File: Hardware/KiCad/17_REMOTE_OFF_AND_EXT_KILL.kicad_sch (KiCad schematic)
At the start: 0 parts

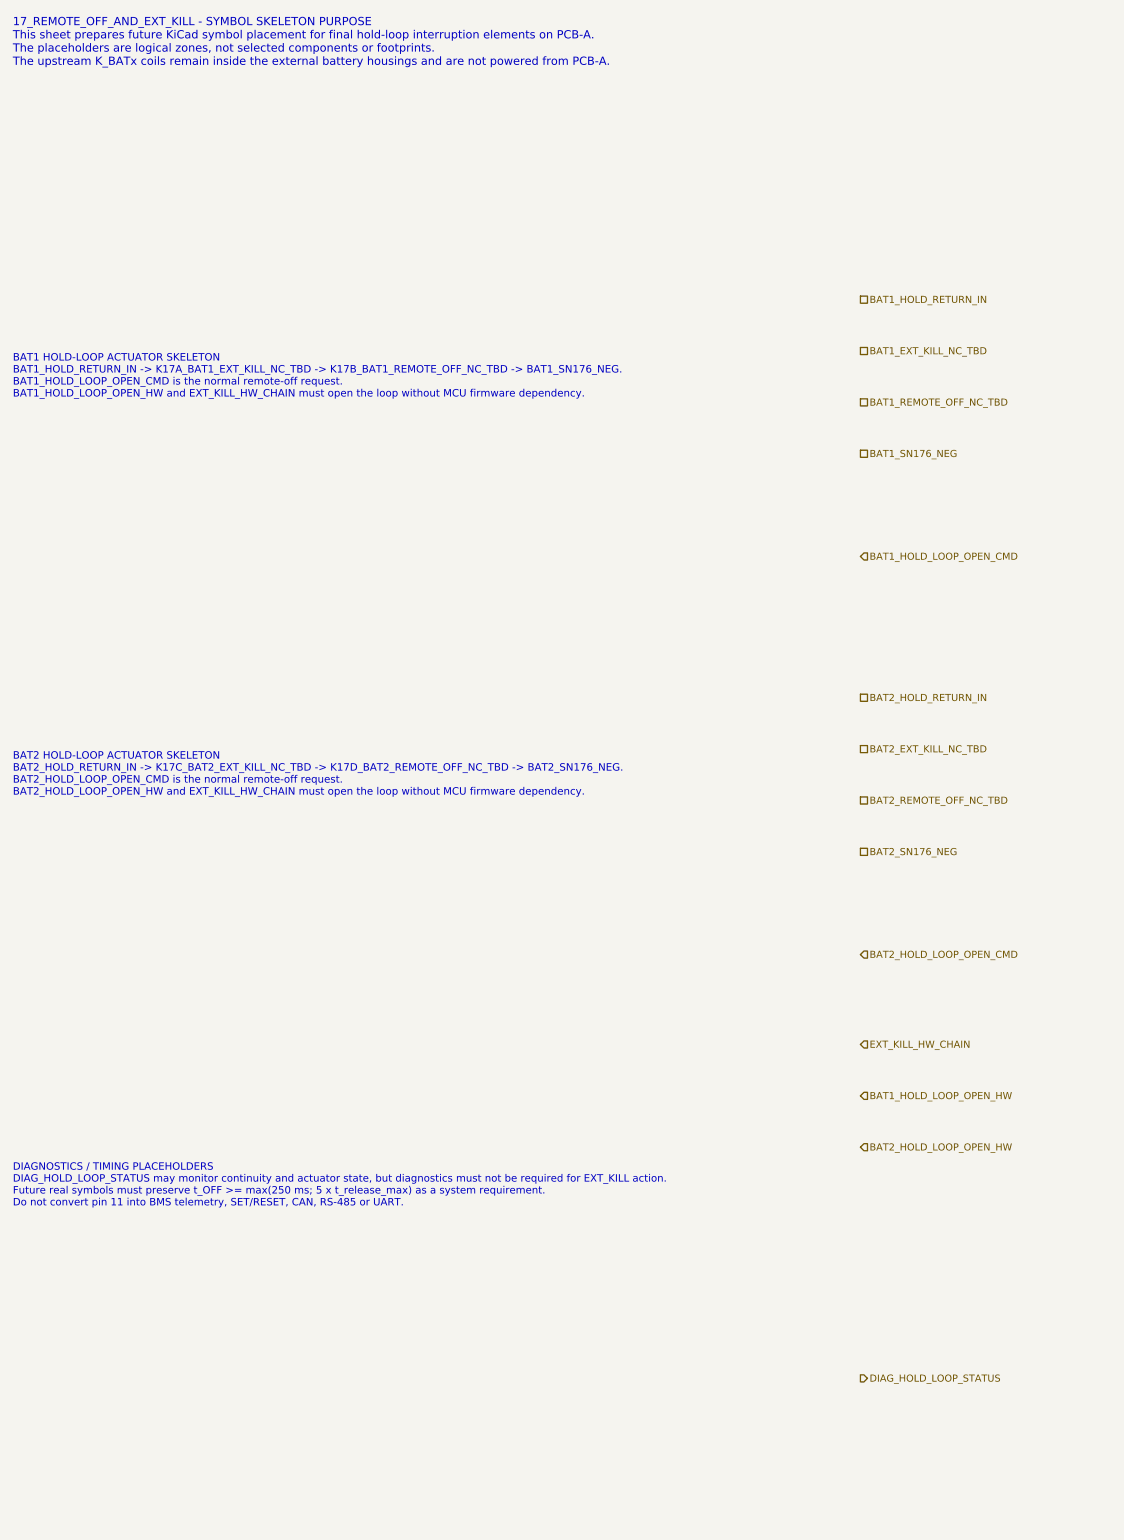
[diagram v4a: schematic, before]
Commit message: hardware: correct REMOTE_OFF physical run-contact semantics
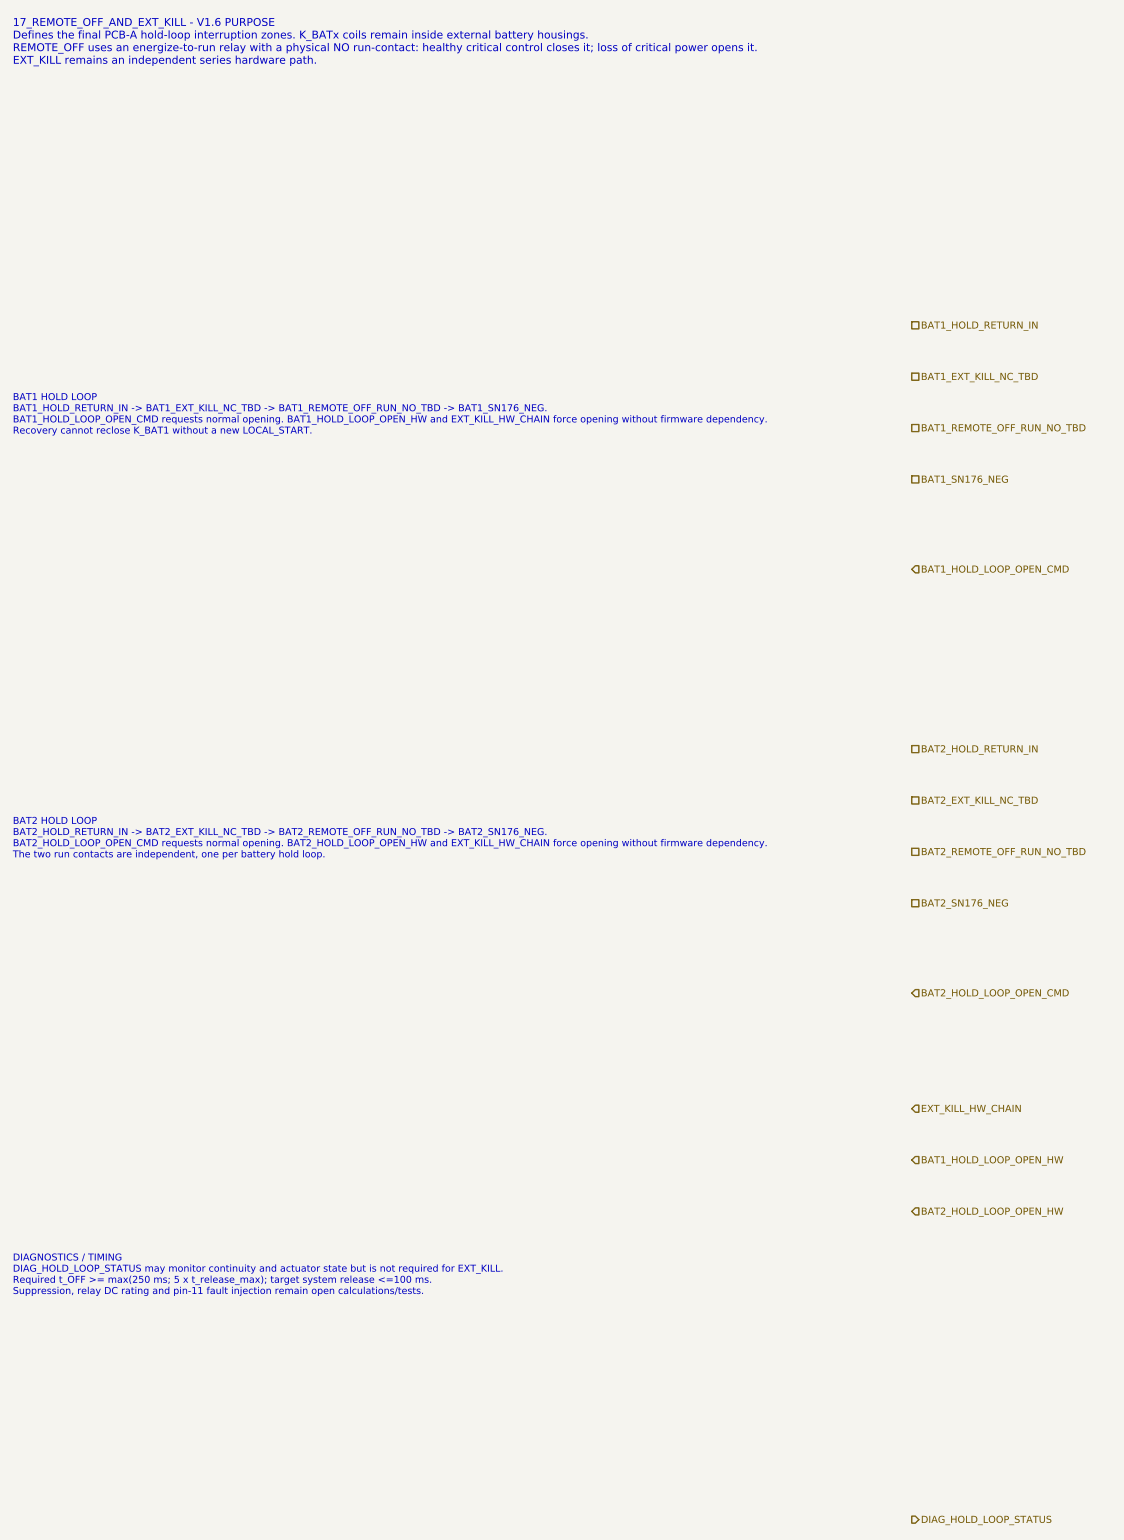
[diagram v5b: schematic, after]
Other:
- note added: "17_REMOTE_OFF_AND_EXT_KILL - V1.6 PURPOSE Defines the final PCB-A hold-loop interruption zones. K_BATx coils remain inside external battery housings. REMOTE_OFF uses an energize-to-run relay with a physical NO run-contact: healthy critical control closes it; loss of critical power opens it. EXT_KILL remains an independent series hardware path."
- note added: "BAT1 HOLD LOOP BAT1_HOLD_RETURN_IN -> BAT1_EXT_KILL_NC_TBD -> BAT1_REMOTE_OFF_RUN_NO_TBD -> BAT1_SN176_NEG. BAT1_HOLD_LOOP_OPEN_CMD requests normal opening. BAT1_HOLD_LOOP_OPEN_HW and EXT_KILL_HW_CHAIN force opening without firmware dependency. Recovery cannot reclose K_BAT1 without a new LOCAL_START."
- note added: "BAT2 HOLD LOOP BAT2_HOLD_RETURN_IN -> BAT2_EXT_KILL_NC_TBD -> BAT2_REMOTE_OFF_RUN_NO_TBD -> BAT2_SN176_NEG. BAT2_HOLD_LOOP_OPEN_CMD requests normal opening. BAT2_HOLD_LOOP_OPEN_HW and EXT_KILL_HW_CHAIN force opening without firmware dependency. The two run contacts are independent, one per battery hold loop."
- note added: "DIAGNOSTICS / TIMING DIAG_HOLD_LOOP_STATUS may monitor continuity and actuator state but is not required for EXT_KILL. Required t_OFF >= max(250 ms; 5 x t_release_max); target system release <=100 ms. Suppression, relay DC rating and pin-11 fault injection remain open calculations/tests."
- note removed: "17_REMOTE_OFF_AND_EXT_KILL - SYMBOL SKELETON PURPOSE This sheet prepares future KiCad symbol placement for final hold-loop interruption elements on PCB-A. The placeholders are logical zones, not selected components or footprints. The upstream K_BATx coils remain inside the external battery housings and are not powered from PCB-A."
- note removed: "BAT1 HOLD-LOOP ACTUATOR SKELETON BAT1_HOLD_RETURN_IN -> K17A_BAT1_EXT_KILL_NC_TBD -> K17B_BAT1_REMOTE_OFF_NC_TBD -> BAT1_SN176_NEG. BAT1_HOLD_LOOP_OPEN_CMD is the normal remote-off request. BAT1_HOLD_LOOP_OPEN_HW and EXT_KILL_HW_CHAIN must open the loop without MCU firmware dependency."
- note removed: "BAT2 HOLD-LOOP ACTUATOR SKELETON BAT2_HOLD_RETURN_IN -> K17C_BAT2_EXT_KILL_NC_TBD -> K17D_BAT2_REMOTE_OFF_NC_TBD -> BAT2_SN176_NEG. BAT2_HOLD_LOOP_OPEN_CMD is the normal remote-off request. BAT2_HOLD_LOOP_OPEN_HW and EXT_KILL_HW_CHAIN must open the loop without MCU firmware dependency."
- note removed: "DIAGNOSTICS / TIMING PLACEHOLDERS DIAG_HOLD_LOOP_STATUS may monitor continuity and actuator state, but diagnostics must not be required for EXT_KILL action. Future real symbols must preserve t_OFF >= max(250 ms; 5 x t_release_max) as a system requirement. Do not convert pin 11 into BMS telemetry, SET/RESET, CAN, RS-485 or UART."
- title: 17_REMOTE_OFF_AND_EXT_KILL - hold-loop final actuators -> 17_REMOTE_OFF_AND_EXT_KILL - fail-open run contacts and EXT_KILL
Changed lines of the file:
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@@
 	(paper "A3")
 	(title_block
-		(title "17_REMOTE_OFF_AND_EXT_KILL - hold-loop final actuators")
-		(date "2026-07-15")
-		(rev "C2")
+		(title "17_REMOTE_OFF_AND_EXT_KILL - fail-open run contacts and EXT_KILL")
+		(date "2026-07-16")
+		(rev "C3")
 		(company "Gonoboben/plataVM")
-		(comment 1 "Interface consistency: canonical hold-loop commands and branch-specific hardware-open actions")
-		(comment 2 "Text-only placeholders; no relay, MOSFET, optocoupler or driver topology selected")
+		(comment 1 "V1.6 corrected physical semantics: energize-to-run NO REMOTE_OFF contacts")
+		(comment 2 "Text-only placeholders; relay, EXT_KILL contact, suppression and diagnostics parts remain unselected")
 	)
-	(text "17_REMOTE_OFF_AND_EXT_KILL - SYMBOL SKELETON PURPOSE\nThis sheet prepares future KiCad symbol placement for final hold-loop interruption elements on PCB-A.\nThe placeholders are logical zones, not selected components or footprints.\nThe upstream K_BATx coils remain inside the external battery housings and are not powered from PCB-A."
+	(text "17_REMOTE_OFF_AND_EXT_KILL - V1.6 PURPOSE\nDefines the final PCB-A hold-loop interruption zones. K_BATx coils remain inside external battery housings.\nREMOTE_OFF uses an energize-to-run relay with a physical NO run-contact: healthy critical control closes it; loss of critical power opens it.\nEXT_KILL remains an independent series hardware path."
 		(exclude_from_sim no)
 		(at 12 14 0)
-		(effects (font (size 1.28 1.28)) (justify left))
-		(uuid "bfe-symbol-00000017-0000-4000-8000-000000000101")
+		(effects (font (size 1.22 1.22)) (justify left))
+		(uuid "roff-v16-17-101")
 	)
-	(text "BAT1 HOLD-LOOP ACTUATOR SKELETON\nBAT1_HOLD_RETURN_IN -> K17A_BAT1_EXT_KILL_NC_TBD -> K17B_BAT1_REMOTE_OFF_NC_TBD -> BAT1_SN176_NEG.\nBAT1_HOLD_LOOP_OPEN_CMD is the normal remote-off request.\nBAT1_HOLD_LOOP_OPEN_HW and EXT_KILL_HW_CHAIN must open the loop without MCU firmware dependency."
+	(text "BAT1 HOLD LOOP\nBAT1_HOLD_RETURN_IN -> BAT1_EXT_KILL_NC_TBD -> BAT1_REMOTE_OFF_RUN_NO_TBD -> BAT1_SN176_NEG.\nBAT1_HOLD_LOOP_OPEN_CMD requests normal opening. BAT1_HOLD_LOOP_OPEN_HW and EXT_KILL_HW_CHAIN force opening without firmware dependency.\nRecovery cannot reclose K_BAT1 without a new LOCAL_START."
 		(exclude_from_sim no)
-		(at 12 66 0)
-		(effects (font (size 1.16 1.16)) (justify left))
-		(uuid "bfe-symbol-00000017-0000-4000-8000-000000000102")
+		(at 12 72 0)
+		(effects (font (size 1.08 1.08)) (justify left))
+		(uuid "roff-v16-17-102")
 	)
-	(text "BAT2 HOLD-LOOP ACTUATOR SKELETON\nBAT2_HOLD_RETURN_IN -> K17C_BAT2_EXT_KILL_NC_TBD -> K17D_BAT2_REMOTE_OFF_NC_TBD -> BAT2_SN176_NEG.\nBAT2_HOLD_LOOP_OPEN_CMD is the normal remote-off request.\nBAT2_HOLD_LOOP_OPEN_HW and EXT_KILL_HW_CHAIN must open the loop without MCU firmware dependency."
+	(text "BAT2 HOLD LOOP\nBAT2_HOLD_RETURN_IN -> BAT2_EXT_KILL_NC_TBD -> BAT2_REMOTE_OFF_RUN_NO_TBD -> BAT2_SN176_NEG.\nBAT2_HOLD_LOOP_OPEN_CMD requests normal opening. BAT2_HOLD_LOOP_OPEN_HW and EXT_KILL_HW_CHAIN force opening without firmware dependency.\nThe two run contacts are independent, one per battery hold loop."
 		(exclude_from_sim no)
-		(at 12 128 0)
-		(effects (font (size 1.16 1.16)) (justify left))
-		(uuid "bfe-symbol-00000017-0000-4000-8000-000000000103")
+		(at 12 138 0)
+		(effects (font (size 1.08 1.08)) (justify left))
+		(uuid "roff-v16-17-103")
 	)
-	(text "DIAGNOSTICS / TIMING PLACEHOLDERS\nDIAG_HOLD_LOOP_STATUS may monitor continuity and actuator state, but diagnostics must not be required for EXT_KILL action.\nFuture real symbols must preserve t_OFF >= max(250 ms; 5 x t_release_max) as a system requirement.\nDo not convert pin 11 into BMS telemetry, SET/RESET, CAN, RS-485 or UART."
+	(text "DIAGNOSTICS / TIMING\nDIAG_HOLD_LOOP_STATUS may monitor continuity and actuator state but is not required for EXT_KILL.\nRequired t_OFF >= max(250 ms; 5 x t_release_max); target system release <=100 ms.\nSuppression, relay DC rating and pin-11 fault injection remain open calculations/tests."
 		(exclude_from_sim no)
-		(at 12 192 0)
-		(effects (font (size 1.15 1.15)) (justify left))
-		(uuid "bfe-symbol-00000017-0000-4000-8000-000000000104")
+		(at 12 206 0)
+		(effects (font (size 1.08 1.08)) (justify left))
+		(uuid "roff-v16-17-104")
 	)
-	(hierarchical_label "BAT1_HOLD_RETURN_IN" (shape passive) (exclude_from_sim no) (at 144 54 0) (effects (font (size 1.1 1.1)) (justify left)) (uuid "bfe-symbol-00000017-0000-4000-8000-000000000201"))
-	(hierarchical_label "BAT1_EXT_KILL_NC_TBD" (shape passive) (exclude_from_sim no) (at 144 62 0) (effects (font (size 1.1 1.1)) (justify left)) (uuid "bfe-symbol-00000017-0000-4000-8000-000000000202"))
-	(hierarchical_label "BAT1_REMOTE_OFF_NC_TBD" (shape passive) (exclude_from_sim no) (at 144 70 0) (effects (font (size 1.1 1.1)) (justify left)) (uuid "bfe-symbol-00000017-0000-4000-8000-000000000203"))
-	(hierarchical_label "BAT1_SN176_NEG" (shape passive) (exclude_from_sim no) (at 144 78 0) (effects (font (size 1.1 1.1)) (justify left)) (uuid "bfe-symbol-00000017-0000-4000-8000-000000000204"))
-	(hierarchical_label "BAT2_HOLD_RETURN_IN" (shape passive) (exclude_from_sim no) (at 144 116 0) (effects (font (size 1.1 1.1)) (justify left)) (uuid "bfe-symbol-00000017-0000-4000-8000-000000000205"))
-	(hierarchical_label "BAT2_EXT_KILL_NC_TBD" (shape passive) (exclude_from_sim no) (at 144 124 0) (effects (font (size 1.1 1.1)) (justify left)) (uuid "bfe-symbol-00000017-0000-4000-8000-000000000206"))
-	(hierarchical_label "BAT2_REMOTE_OFF_NC_TBD" (shape passive) (exclude_from_sim no) (at 144 132 0) (effects (font (size 1.1 1.1)) (justify left)) (uuid "bfe-symbol-00000017-0000-4000-8000-000000000207"))
-	(hierarchical_label "BAT2_SN176_NEG" (shape passive) (exclude_from_sim no) (at 144 140 0) (effects (font (size 1.1 1.1)) (justify left)) (uuid "bfe-symbol-00000017-0000-4000-8000-000000000208"))
-	(hierarchical_label "BAT1_HOLD_LOOP_OPEN_CMD" (shape input) (exclude_from_sim no) (at 144 94 0) (effects (font (size 1.1 1.1)) (justify left)) (uuid "bfe-symbol-00000017-0000-4000-8000-000000000209"))
-	(hierarchical_label "BAT2_HOLD_LOOP_OPEN_CMD" (shape input) (exclude_from_sim no) (at 144 156 0) (effects (font (size 1.1 1.1)) (justify left)) (uuid "bfe-symbol-00000017-0000-4000-8000-000000000210"))
-	(hierarchical_label "EXT_KILL_HW_CHAIN" (shape input) (exclude_from_sim no) (at 144 170 0) (effects (font (size 1.1 1.1)) (justify left)) (uuid "bfe-symbol-00000017-0000-4000-8000-000000000211"))
-	(hierarchical_label "BAT1_HOLD_LOOP_OPEN_HW" (shape input) (exclude_from_sim no) (at 144 178 0) (effects (font (size 1.1 1.1)) (justify left)) (uuid "bfe-symbol-00000017-0000-4000-8000-000000000213"))
-	(hierarchical_label "BAT2_HOLD_LOOP_OPEN_HW" (shape input) (exclude_from_sim no) (at 144 186 0) (effects (font (size 1.1 1.1)) (justify left)) (uuid "bfe-symbol-00000017-0000-4000-8000-000000000214"))
-	(hierarchical_label "DIAG_HOLD_LOOP_STATUS" (shape output) (exclude_from_sim no) (at 144 222 0) (effects (font (size 1.1 1.1)) (justify left)) (uuid "bfe-symbol-00000017-0000-4000-8000-000000000212"))
+	(hierarchical_label "BAT1_HOLD_RETURN_IN" (shape passive) (exclude_from_sim no) (at 152 58 0) (effects (font (size 1.1 1.1)) (justify left)) (uuid "roff-v16-17-201"))
+	(hierarchical_label "BAT1_EXT_KILL_NC_TBD" (shape passive) (exclude_from_sim no) (at 152 66 0) (effects (font (size 1.1 1.1)) (justify left)) (uuid "roff-v16-17-202"))
+	(hierarchical_label "BAT1_REMOTE_OFF_RUN_NO_TBD" (shape passive) (exclude_from_sim no) (at 152 74 0) (effects (font (size 1.1 1.1)) (justify left)) (uuid "roff-v16-17-203"))
+	(hierarchical_label "BAT1_SN176_NEG" (shape passive) (exclude_from_sim no) (at 152 82 0) (effects (font (size 1.1 1.1)) (justify left)) (uuid "roff-v16-17-204"))
+	(hierarchical_label "BAT2_HOLD_RETURN_IN" (shape passive) (exclude_from_sim no) (at 152 124 0) (effects (font (size 1.1 1.1)) (justify left)) (uuid "roff-v16-17-205"))
+	(hierarchical_label "BAT2_EXT_KILL_NC_TBD" (shape passive) (exclude_from_sim no) (at 152 132 0) (effects (font (size 1.1 1.1)) (justify left)) (uuid "roff-v16-17-206"))
+	(hierarchical_label "BAT2_REMOTE_OFF_RUN_NO_TBD" (shape passive) (exclude_from_sim no) (at 152 140 0) (effects (font (size 1.1 1.1)) (justify left)) (uuid "roff-v16-17-207"))
+	(hierarchical_label "BAT2_SN176_NEG" (shape passive) (exclude_from_sim no) (at 152 148 0) (effects (font (size 1.1 1.1)) (justify left)) (uuid "roff-v16-17-208"))
+	(hierarchical_label "BAT1_HOLD_LOOP_OPEN_CMD" (shape input) (exclude_from_sim no) (at 152 96 0) (effects (font (size 1.1 1.1)) (justify left)) (uuid "roff-v16-17-209"))
+	(hierarchical_label "BAT2_HOLD_LOOP_OPEN_CMD" (shape input) (exclude_from_sim no) (at 152 162 0) (effects (font (size 1.1 1.1)) (justify left)) (uuid "roff-v16-17-210"))
+	(hierarchical_label "EXT_KILL_HW_CHAIN" (shape input) (exclude_from_sim no) (at 152 180 0) (effects (font (size 1.1 1.1)) (justify left)) (uuid "roff-v16-17-211"))
+	(hierarchical_label "BAT1_HOLD_LOOP_OPEN_HW" (shape input) (exclude_from_sim no) (at 152 188 0) (effects (font (size 1.1 1.1)) (justify left)) (uuid "roff-v16-17-212"))
+	(hierarchical_label "BAT2_HOLD_LOOP_OPEN_HW" (shape input) (exclude_from_sim no) (at 152 196 0) (effects (font (size 1.1 1.1)) (justify left)) (uuid "roff-v16-17-213"))
+	(hierarchical_label "DIAG_HOLD_LOOP_STATUS" (shape output) (exclude_from_sim no) (at 152 244 0) (effects (font (size 1.1 1.1)) (justify left)) (uuid "roff-v16-17-214"))
 )
